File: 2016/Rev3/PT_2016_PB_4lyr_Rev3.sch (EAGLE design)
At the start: 167 parts, among them Q1 MOSFET-NCHANNELFDD8780, Q12 2N7002, Q2 MMBT2222A, Q3 MOSFET-NCHANNELFDD8780, Q4 MMBT2222A

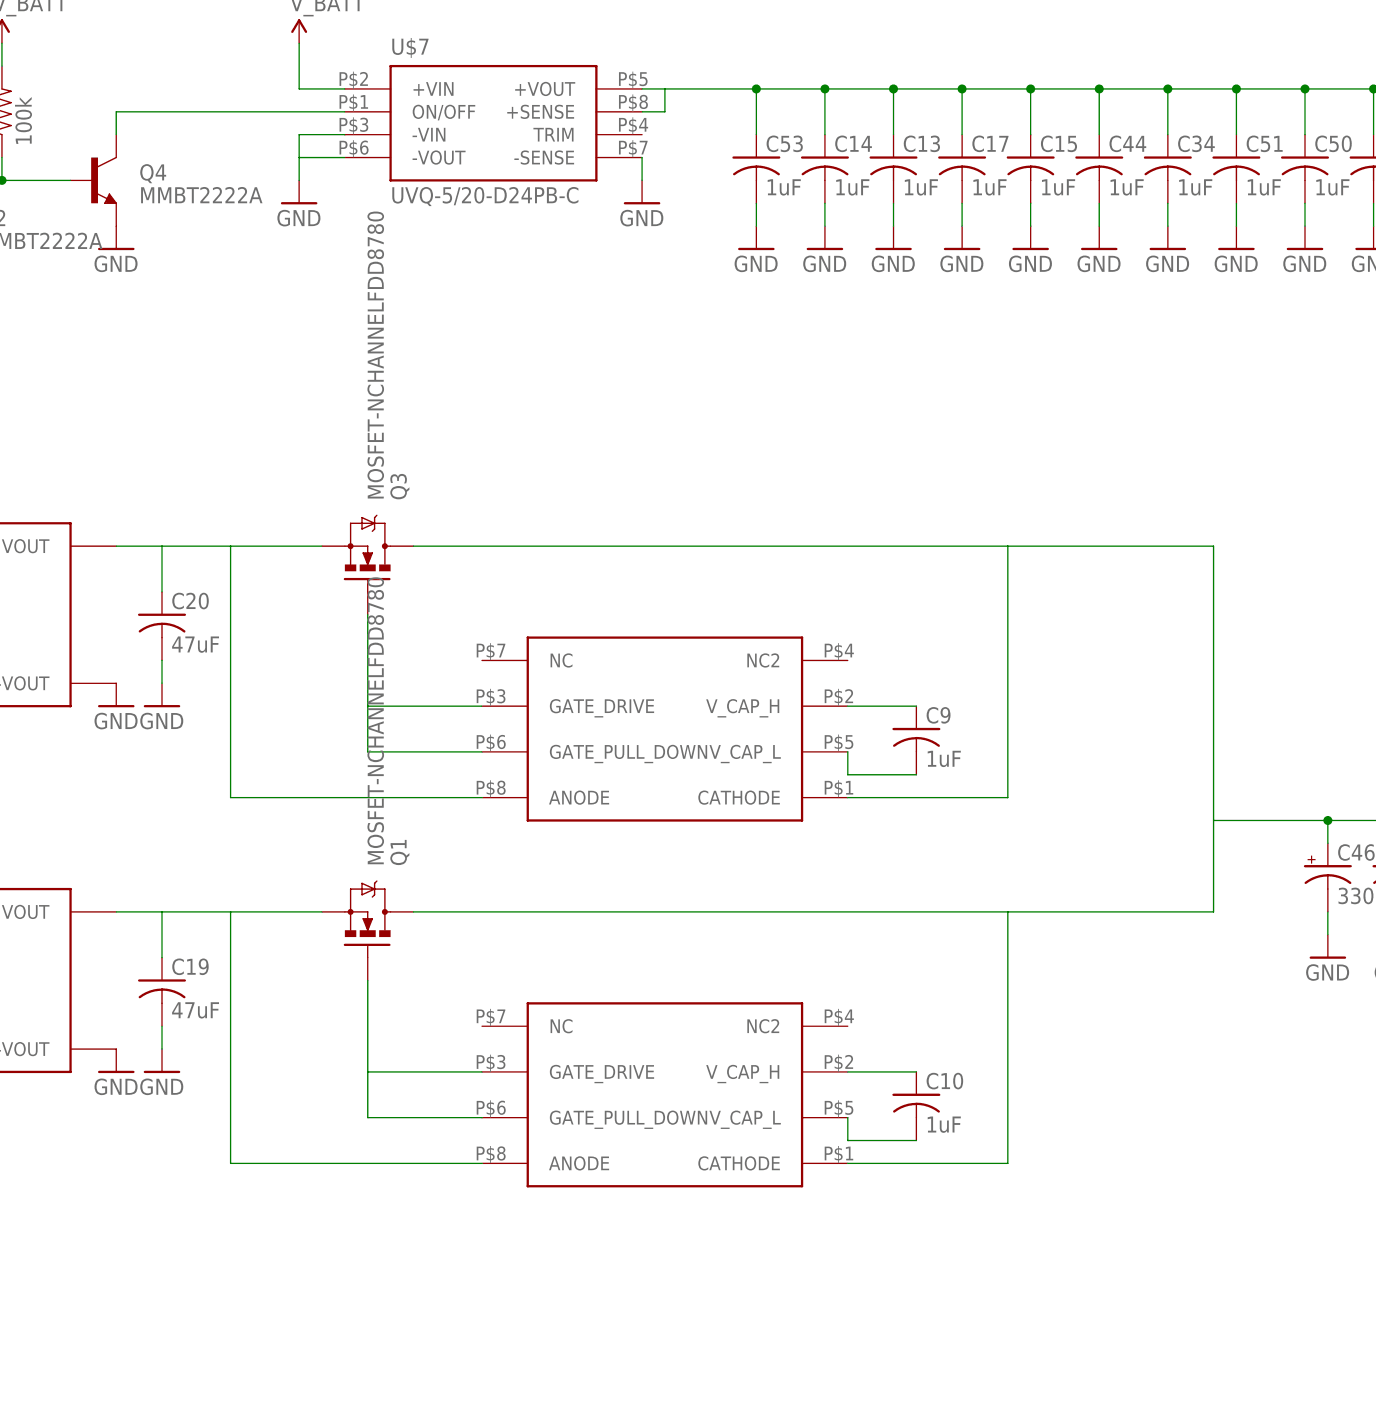
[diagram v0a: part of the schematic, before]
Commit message: Swapped LM74670 with LM5050
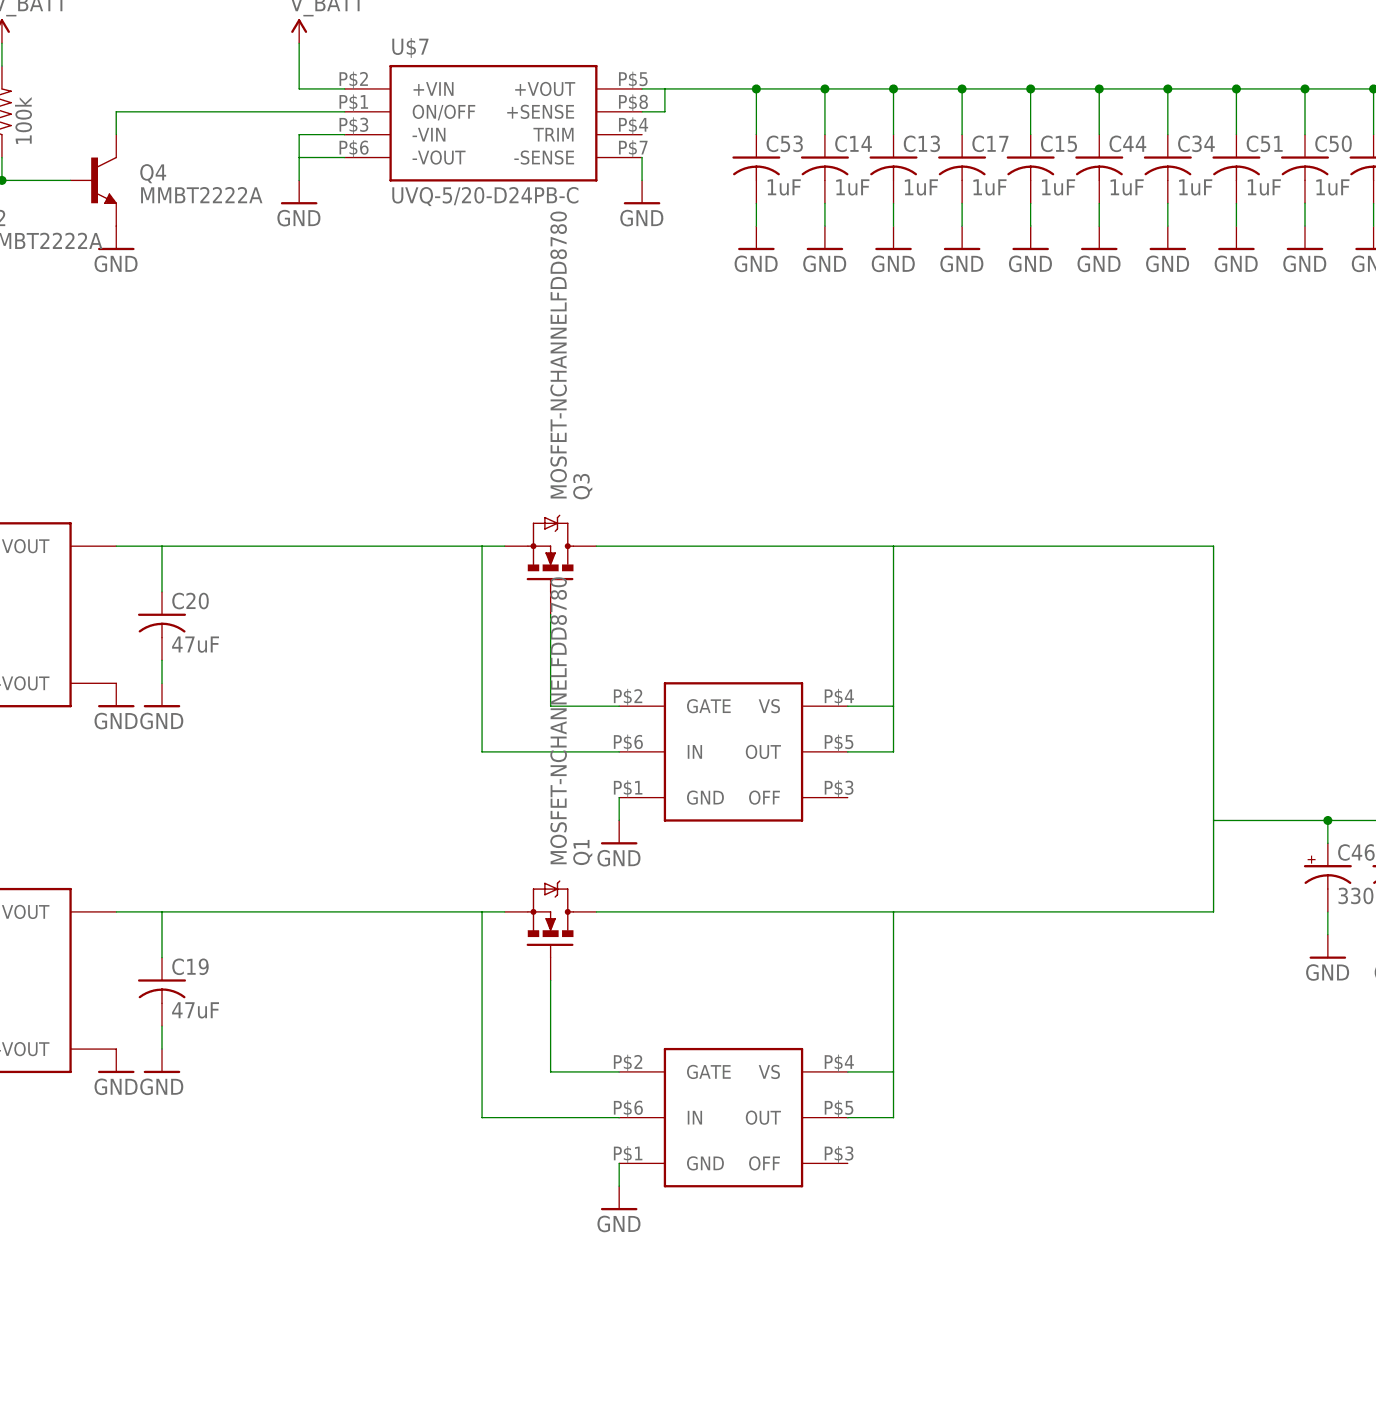
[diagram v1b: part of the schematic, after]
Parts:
- removed C10, C9: 1uF, resistor:C-USC1206
- removed U$13: LM74670-Q1, LM74670-Q1:LM74670-Q1
- added U$6: LM5050, LM5050:LM5050
- U$9: value LM74670-Q1 -> LM5050; device LM74670-Q1:LM74670-Q1 -> LM5050:LM5050
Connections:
- removed net N$10: C10.2, U$13.V_CAP_L
- removed net N$7: C9.1, U$9.V_CAP_H
- removed net N$8: C9.2, U$9.V_CAP_L
- removed net N$9: C10.1, U$13.V_CAP_H
- net GND: now also U$6.GND, U$9.GND
- net N$1: now also U$6.IN; no longer U$9.ANODE
- net N$2: now also U$9.IN; no longer U$13.ANODE
- net N$3: now also U$6.GATE; no longer U$9.GATE_DRIVE, U$9.GATE_PULL_DOWN
- net N$33: now also U$6.OUT, U$6.VS, U$9.OUT, U$9.VS; no longer U$13.CATHODE, U$9.CATHODE
- net N$5: now also U$9.GATE; no longer U$13.GATE_DRIVE, U$13.GATE_PULL_DOWN
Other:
- moved on the sheet: Q1, Q3
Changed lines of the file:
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@@
 <part name="R5" library="resistor" deviceset="R-US_" device="R1206" value="100k"/>
 <part name="GND91" library="SparkFun-Aesthetics" deviceset="GND" device=""/>
-<part name="U$9" library="LM74670-Q1" deviceset="LM74670-Q1" device=""/>
-<part name="U$13" library="LM74670-Q1" deviceset="LM74670-Q1" device=""/>
 <part name="Q1" library="SparkFun-DiscreteSemi" deviceset="MOSFET-NCHANNEL" device="FDD8780"/>
 <part name="Q3" library="SparkFun-DiscreteSemi" deviceset="MOSFET-NCHANNEL" device="FDD8780"/>
-<part name="C9" library="resistor" deviceset="C-US" device="C1206" value="1uF"/>
-<part name="C10" library="resistor" deviceset="C-US" device="C1206" value="1uF"/>
 <part name="SUPPLY31" library="SparkFun-Aesthetics" deviceset="5V" device=""/>
 <part name="Q4" library="SparkFun-DiscreteSemi" deviceset="TRANSISTOR_NPN" device="MMBT2222A" value="MMBT2222A"/>
@@
 <part name="R6" library="SparkFun-Passives" deviceset="RESISTOR" device="1206" value="100k"/>
 <part name="GND35" library="SparkFun-Aesthetics" deviceset="GND" device=""/>
+<part name="U$6" library="LM5050" deviceset="LM5050" device=""/>
+<part name="U$9" library="LM5050" deviceset="LM5050" device=""/>
+<part name="GND92" library="SparkFun-Aesthetics" deviceset="GND" device=""/>
+<part name="GND93" library="SparkFun-Aesthetics" deviceset="GND" device=""/>
 </parts>
 <sheets>
@@
 <instance part="R5" gate="G$1" x="-132.08" y="38.1" rot="R270"/>
 <instance part="GND91" gate="1" x="-132.08" y="30.48"/>
-<instance part="U$9" gate="G$1" x="35.56" y="58.42"/>
-<instance part="U$13" gate="G$1" x="35.56" y="17.78"/>
-<instance part="Q1" gate="G$1" x="2.54" y="40.64" rot="MR90"/>
-<instance part="Q3" gate="G$1" x="2.54" y="81.28" rot="MR90"/>
-<instance part="C9" gate="G$1" x="63.5" y="60.96"/>
-<instance part="C10" gate="G$1" x="63.5" y="20.32"/>
+<instance part="Q1" gate="G$1" x="22.86" y="40.64" rot="MR90"/>
+<instance part="Q3" gate="G$1" x="22.86" y="81.28" rot="MR90"/>
 <instance part="SUPPLY31" gate="G$1" x="200.66" y="-76.2"/>
 <instance part="Q4" gate="G$1" x="-27.94" y="121.92"/>
@@
 <instance part="R6" gate="G$1" x="-50.8" y="109.22" rot="R270"/>
 <instance part="GND35" gate="1" x="-50.8" y="101.6"/>
+<instance part="U$6" gate="G$1" x="40.64" y="58.42"/>
+<instance part="U$9" gate="G$1" x="40.64" y="17.78"/>
+<instance part="GND92" gate="1" x="30.48" y="48.26"/>
+<instance part="GND93" gate="1" x="30.48" y="7.62"/>
 </instances>
 <busses>
@@
 <pinref part="R6" gate="G$1" pin="2"/>
 <pinref part="GND35" gate="1" pin="GND"/>
+</segment>
+<segment>
+<pinref part="U$6" gate="G$1" pin="GND"/>
+<pinref part="GND92" gate="1" pin="GND"/>
+<wire x1="30.48" y1="53.34" x2="30.48" y2="50.8" width="0.1524" layer="91"/>
+</segment>
+<segment>
+<pinref part="U$9" gate="G$1" pin="GND"/>
+<pinref part="GND93" gate="1" pin="GND"/>
+<wire x1="30.48" y1="12.7" x2="30.48" y2="10.16" width="0.1524" layer="91"/>
 </segment>
 </net>
@@
 <junction x="116.84" y="50.8"/>
 <pinref part="Q3" gate="G$1" pin="D"/>
-<wire x1="7.62" y1="81.28" x2="73.66" y2="81.28" width="0.1524" layer="91"/>
-<pinref part="U$9" gate="G$1" pin="CATHODE"/>
-<wire x1="73.66" y1="81.28" x2="96.52" y2="81.28" width="0.1524" layer="91"/>
-<wire x1="55.88" y1="53.34" x2="73.66" y2="53.34" width="0.1524" layer="91"/>
-<wire x1="73.66" y1="53.34" x2="73.66" y2="81.28" width="0.1524" layer="91"/>
+<wire x1="27.94" y1="81.28" x2="60.96" y2="81.28" width="0.1524" layer="91"/>
 <pinref part="Q1" gate="G$1" pin="D"/>
-<wire x1="7.62" y1="40.64" x2="73.66" y2="40.64" width="0.1524" layer="91"/>
-<wire x1="73.66" y1="40.64" x2="96.52" y2="40.64" width="0.1524" layer="91"/>
+<wire x1="60.96" y1="81.28" x2="96.52" y2="81.28" width="0.1524" layer="91"/>
+<wire x1="27.94" y1="40.64" x2="60.96" y2="40.64" width="0.1524" layer="91"/>
+<wire x1="60.96" y1="40.64" x2="96.52" y2="40.64" width="0.1524" layer="91"/>
 <wire x1="96.52" y1="40.64" x2="96.52" y2="50.8" width="0.1524" layer="91"/>
-<pinref part="U$13" gate="G$1" pin="CATHODE"/>
-<wire x1="55.88" y1="12.7" x2="73.66" y2="12.7" width="0.1524" layer="91"/>
-<wire x1="73.66" y1="12.7" x2="73.66" y2="40.64" width="0.1524" layer="91"/>
+<pinref part="U$6" gate="G$1" pin="VS"/>
+<wire x1="55.88" y1="63.5" x2="60.96" y2="63.5" width="0.1524" layer="91"/>
+<wire x1="60.96" y1="63.5" x2="60.96" y2="81.28" width="0.1524" layer="91"/>
+<pinref part="U$6" gate="G$1" pin="OUT"/>
+<wire x1="55.88" y1="58.42" x2="60.96" y2="58.42" width="0.1524" layer="91"/>
+<wire x1="60.96" y1="58.42" x2="60.96" y2="63.5" width="0.1524" layer="91"/>
+<pinref part="U$9" gate="G$1" pin="VS"/>
+<wire x1="55.88" y1="22.86" x2="60.96" y2="22.86" width="0.1524" layer="91"/>
+<wire x1="60.96" y1="22.86" x2="60.96" y2="40.64" width="0.1524" layer="91"/>
+<pinref part="U$9" gate="G$1" pin="OUT"/>
+<wire x1="55.88" y1="17.78" x2="60.96" y2="17.78" width="0.1524" layer="91"/>
+<wire x1="60.96" y1="17.78" x2="60.96" y2="22.86" width="0.1524" layer="91"/>
 </segment>
 </net>
@@
 <pinref part="Q3" gate="G$1" pin="S"/>
 <wire x1="-25.4" y1="81.28" x2="-20.32" y2="81.28" width="0.1524" layer="91"/>
-<pinref part="U$9" gate="G$1" pin="ANODE"/>
-<wire x1="-20.32" y1="81.28" x2="-12.7" y2="81.28" width="0.1524" layer="91"/>
-<wire x1="-12.7" y1="81.28" x2="-2.54" y2="81.28" width="0.1524" layer="91"/>
-<wire x1="15.24" y1="53.34" x2="-12.7" y2="53.34" width="0.1524" layer="91"/>
-<wire x1="-12.7" y1="53.34" x2="-12.7" y2="81.28" width="0.1524" layer="91"/>
+<wire x1="-20.32" y1="81.28" x2="15.24" y2="81.28" width="0.1524" layer="91"/>
 <pinref part="C20" gate="G$1" pin="1"/>
+<wire x1="15.24" y1="81.28" x2="17.78" y2="81.28" width="0.1524" layer="91"/>
 <wire x1="-20.32" y1="76.2" x2="-20.32" y2="81.28" width="0.1524" layer="91"/>
+<pinref part="U$6" gate="G$1" pin="IN"/>
+<wire x1="30.48" y1="58.42" x2="15.24" y2="58.42" width="0.1524" layer="91"/>
+<wire x1="15.24" y1="58.42" x2="15.24" y2="81.28" width="0.1524" layer="91"/>
 </segment>
 </net>
@@
 <pinref part="Q1" gate="G$1" pin="S"/>
 <wire x1="-25.4" y1="40.64" x2="-20.32" y2="40.64" width="0.1524" layer="91"/>
-<pinref part="U$13" gate="G$1" pin="ANODE"/>
-<wire x1="-20.32" y1="40.64" x2="-12.7" y2="40.64" width="0.1524" layer="91"/>
-<wire x1="-12.7" y1="40.64" x2="-2.54" y2="40.64" width="0.1524" layer="91"/>
-<wire x1="15.24" y1="12.7" x2="-12.7" y2="12.7" width="0.1524" layer="91"/>
-<wire x1="-12.7" y1="12.7" x2="-12.7" y2="40.64" width="0.1524" layer="91"/>
+<wire x1="-20.32" y1="40.64" x2="15.24" y2="40.64" width="0.1524" layer="91"/>
 <pinref part="C19" gate="G$1" pin="1"/>
+<wire x1="15.24" y1="40.64" x2="17.78" y2="40.64" width="0.1524" layer="91"/>
 <wire x1="-20.32" y1="35.56" x2="-20.32" y2="40.64" width="0.1524" layer="91"/>
-</segment>
-</net>
-<net name="N$3" class="0">
-<segment>
-<pinref part="U$9" gate="G$1" pin="GATE_PULL_DOWN"/>
-<pinref part="Q3" gate="G$1" pin="G"/>
-<wire x1="15.24" y1="58.42" x2="2.54" y2="58.42" width="0.1524" layer="91"/>
-<wire x1="2.54" y1="58.42" x2="2.54" y2="63.5" width="0.1524" layer="91"/>
-<pinref part="U$9" gate="G$1" pin="GATE_DRIVE"/>
-<wire x1="2.54" y1="63.5" x2="2.54" y2="73.66" width="0.1524" layer="91"/>
-<wire x1="15.24" y1="63.5" x2="2.54" y2="63.5" width="0.1524" layer="91"/>
-</segment>
-</net>
-<net name="N$5" class="0">
-<segment>
-<pinref part="U$13" gate="G$1" pin="GATE_PULL_DOWN"/>
-<pinref part="Q1" gate="G$1" pin="G"/>
-<wire x1="15.24" y1="17.78" x2="2.54" y2="17.78" width="0.1524" layer="91"/>
-<wire x1="2.54" y1="17.78" x2="2.54" y2="22.86" width="0.1524" layer="91"/>
-<wire x1="2.54" y1="33.02" x2="2.54" y2="22.86" width="0.1524" layer="91"/>
-<pinref part="U$13" gate="G$1" pin="GATE_DRIVE"/>
-<wire x1="2.54" y1="22.86" x2="15.24" y2="22.86" width="0.1524" layer="91"/>
-</segment>
-</net>
-<net name="N$7" class="0">
-<segment>
-<pinref part="U$9" gate="G$1" pin="V_CAP_H"/>
-<pinref part="C9" gate="G$1" pin="1"/>
-<wire x1="55.88" y1="63.5" x2="63.5" y2="63.5" width="0.1524" layer="91"/>
-</segment>
-</net>
-<net name="N$8" class="0">
-<segment>
-<pinref part="U$9" gate="G$1" pin="V_CAP_L"/>
-<wire x1="55.88" y1="58.42" x2="55.88" y2="55.88" width="0.1524" layer="91"/>
-<pinref part="C9" gate="G$1" pin="2"/>
-<wire x1="55.88" y1="55.88" x2="63.5" y2="55.88" width="0.1524" layer="91"/>
-</segment>
-</net>
-<net name="N$9" class="0">
-<segment>
-<pinref part="U$13" gate="G$1" pin="V_CAP_H"/>
-<pinref part="C10" gate="G$1" pin="1"/>
-<wire x1="55.88" y1="22.86" x2="63.5" y2="22.86" width="0.1524" layer="91"/>
-</segment>
-</net>
-<net name="N$10" class="0">
-<segment>
-<pinref part="U$13" gate="G$1" pin="V_CAP_L"/>
-<wire x1="55.88" y1="17.78" x2="55.88" y2="15.24" width="0.1524" layer="91"/>
-<pinref part="C10" gate="G$1" pin="2"/>
-<wire x1="55.88" y1="15.24" x2="63.5" y2="15.24" width="0.1524" layer="91"/>
+<pinref part="U$9" gate="G$1" pin="IN"/>
+<wire x1="30.48" y1="17.78" x2="15.24" y2="17.78" width="0.1524" layer="91"/>
+<wire x1="15.24" y1="17.78" x2="15.24" y2="40.64" width="0.1524" layer="91"/>
 </segment>
 </net>
@@
 </segment>
 </net>
+<net name="N$3" class="0">
+<segment>
+<pinref part="U$6" gate="G$1" pin="GATE"/>
+<pinref part="Q3" gate="G$1" pin="G"/>
+<wire x1="30.48" y1="63.5" x2="22.86" y2="63.5" width="0.1524" layer="91"/>
+<wire x1="22.86" y1="63.5" x2="22.86" y2="73.66" width="0.1524" layer="91"/>
+</segment>
+</net>
+<net name="N$5" class="0">
+<segment>
+<pinref part="U$9" gate="G$1" pin="GATE"/>
+<pinref part="Q1" gate="G$1" pin="G"/>
+<wire x1="30.48" y1="22.86" x2="22.86" y2="22.86" width="0.1524" layer="91"/>
+<wire x1="22.86" y1="22.86" x2="22.86" y2="33.02" width="0.1524" layer="91"/>
+</segment>
+</net>
